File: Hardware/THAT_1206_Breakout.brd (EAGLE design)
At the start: 45.7 x 20.3 mm, 32 parts, among them IC1 THAT1206, J1 INPUT, J2 CHASSIS, J3 RN, J4 TN, J5 SN, J6 1x4, J7 R, J8 T

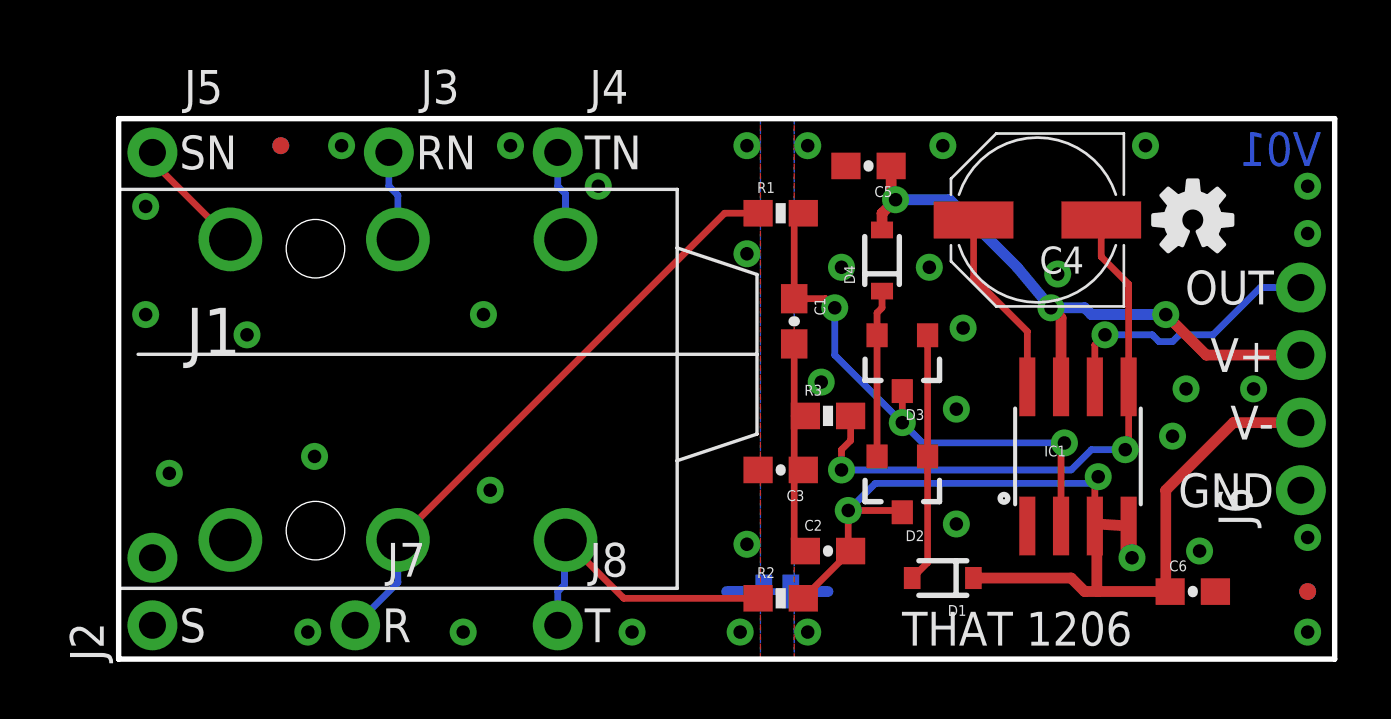
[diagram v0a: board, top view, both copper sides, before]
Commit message: Moving PTH holes to 0.1" grid, matching size to 1646 board.
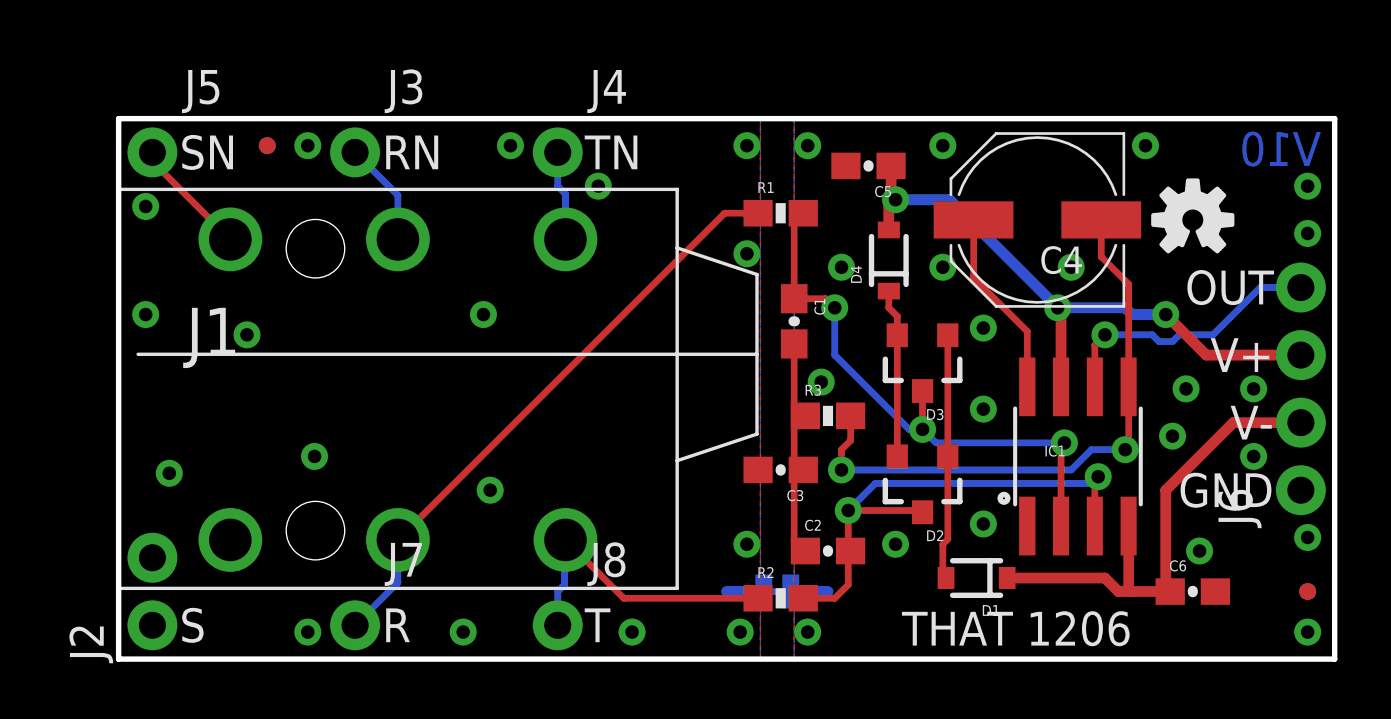
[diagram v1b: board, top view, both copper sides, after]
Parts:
- moved D1 1.27 mm to (32.3, 3.05)
- moved J3 1.27 mm to (8.89, 19.1)
- moved D2 0.76 mm to (30.2, 6.62)
- moved D3 0.76 mm to (30.2, 11.2)
- moved FD2 0.51 mm to (5.59, 19.3)
- moved FD3 0.51 mm to (5.59, 19.3)
- moved D4 0.25 mm to (29.0, 15.0)
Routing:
- net VNEG: track 21.4 -> 18.9 mm
- net N$4: track 18.0 -> 19.4 mm
- net N$10: track 3.41 -> 3.94 mm
- net GND: vias 20 -> 21
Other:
- board text added: "V10"
- board text removed: "V01"

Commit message: Updates after group review.
-Chassis ground moved out of selective solder runout path.
-Flame turned right side up.
-A few via/silk overlaps fixed.
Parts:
- added J9: Chassis, SparkFun-Connectors:1X01_NO_SILK
- J2: value CHASSIS -> S; device SparkFun-Connectors:1X02_NO_SILK -> SparkFun-Connectors:1X01_NO_SILK
- moved LOGO2 4.91 mm to (10.9, 7.62), turned to 0 degrees
- turned J2 to 0 degrees
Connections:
- net GND-ISO: now also J9.1; no longer J2.2
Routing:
- net GND: vias 21 -> 22
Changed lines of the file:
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@@
 <setting verticaltext="up"/>
 </settings>
-<grid distance="0.1" unitdist="inch" unit="inch" style="lines" multiple="1" display="yes" altdistance="0.01" altunitdist="inch" altunit="inch"/>
+<grid distance="0.05" unitdist="inch" unit="inch" style="lines" multiple="1" display="yes" altdistance="0.005" altunitdist="inch" altunit="inch"/>
 <layers>
 <layer number="1" name="Top" color="4" fill="1" visible="yes" active="yes"/>
@@
 <layer number="45" name="Holes" color="7" fill="1" visible="no" active="yes"/>
 <layer number="46" name="Milling" color="3" fill="1" visible="no" active="yes"/>
-<layer number="47" name="Measures" color="7" fill="1" visible="yes" active="yes"/>
+<layer number="47" name="Measures" color="7" fill="1" visible="no" active="yes"/>
 <layer number="48" name="Document" color="7" fill="1" visible="no" active="yes"/>
 <layer number="49" name="Reference" color="7" fill="1" visible="no" active="yes"/>
@@
 Line Receiver
 Breakout</text>
-<text x="1.27" y="4.826" size="1.27" layer="22" font="vector" ratio="15" rot="MR90" align="center-left">Chassis</text>
+<text x="1.27" y="2.54" size="1.27" layer="22" font="vector" ratio="15" rot="MR90" align="center-left">Chassis</text>
 <text x="26.162" y="0.508" size="1.016" layer="22" font="vector" ratio="15" rot="MR0" align="bottom-right">Cut jumper to
 isolate chassis
@@
 <attribute name="PROD_ID" value="CAP-08604" x="40.386" y="2.54" size="1.778" layer="27" font="vector" ratio="15" display="off"/>
 </element>
-<element name="J2" library="SparkFun-Connectors" package="1X02_NO_SILK" value="CHASSIS" x="1.27" y="1.27" rot="R90"/>
 <element name="J6" library="SparkFun-Connectors" package="1X04_NO_SILK_ALL_ROUND" value="1x4" x="44.45" y="6.35" rot="R90">
 <attribute name="PROD_ID" value="CONN-09696" x="44.45" y="6.35" size="1.778" layer="27" font="vector" ratio="15" rot="R90" display="off"/>
@@
 <element name="FD3" library="SparkFun-Aesthetics" package="MICRO-FIDUCIAL" value="FIDUCIALUFIDUCIAL" x="5.588" y="19.304"/>
 <element name="FD4" library="SparkFun-Aesthetics" package="MICRO-FIDUCIAL" value="FIDUCIALUFIDUCIAL" x="44.704" y="2.54"/>
-<element name="LOGO2" library="SparkFun-Aesthetics" package="SFE_LOGO_FLAME_.2" value="SFE_LOGO_FLAME.2_INCH" x="12.7" y="12.192" rot="MR270"/>
+<element name="LOGO2" library="SparkFun-Aesthetics" package="SFE_LOGO_FLAME_.2" value="SFE_LOGO_FLAME.2_INCH" x="10.922" y="7.62" rot="MR0"/>
 <element name="FD1" library="SparkFun-Aesthetics" package="MICRO-FIDUCIAL" value="FIDUCIALUFIDUCIAL" x="44.704" y="2.54" rot="MR0"/>
 <element name="FD2" library="SparkFun-Aesthetics" package="MICRO-FIDUCIAL" value="FIDUCIALUFIDUCIAL" x="5.588" y="19.304" rot="MR90"/>
@@
 <element name="J7" library="SparkFun-Connectors" package="1X01_NO_SILK" value="R" x="8.89" y="1.27"/>
 <element name="J8" library="SparkFun-Connectors" package="1X01_NO_SILK" value="T" x="16.51" y="1.27"/>
+<element name="J2" library="SparkFun-Connectors" package="1X01_NO_SILK" value="S" x="1.27" y="1.27"/>
+<element name="J9" library="SparkFun-Connectors" package="1X01_NO_SILK" value="Chassis" x="1.27" y="11.43"/>
 </elements>
 <signals>
@@
 <via x="32.512" y="12.446" extent="1-16" drill="0.508"/>
 <via x="32.512" y="9.398" extent="1-16" drill="0.508"/>
-<via x="29.21" y="4.318" extent="1-16" drill="0.508"/>
+<via x="28.956" y="3.302" extent="1-16" drill="0.508"/>
 <via x="25.908" y="1.016" extent="1-16" drill="0.508"/>
 <via x="40.64" y="4.064" extent="1-16" drill="0.508"/>
@@
 <via x="26.416" y="10.414" extent="1-16" drill="0.508"/>
 <via x="32.512" y="5.08" extent="1-16" drill="0.508"/>
+<via x="33.147" y="1.524" extent="1-16" drill="0.508"/>
 </signal>
 <signal name="VCC">
@@
 <contactref element="C3" pad="2"/>
 <contactref element="J1" pad="SLEEVE"/>
-<contactref element="J2" pad="2"/>
-<contactref element="J2" pad="1"/>
 <polygon width="0.254" layer="16" isolate="0.3048">
 <vertex x="0" y="20.32"/>
@@
 <via x="7.366" y="7.62" extent="1-16" drill="0.508"/>
 <via x="1.016" y="12.954" extent="1-16" drill="0.508"/>
-<via x="1.905" y="6.985" extent="1-16" drill="0.508"/>
+<via x="2.159" y="7.366" extent="1-16" drill="0.508"/>
 <via x="7.112" y="1.016" extent="1-16" drill="0.508"/>
 <via x="12.954" y="1.016" extent="1-16" drill="0.508"/>
@@
 <via x="14.732" y="19.304" extent="1-16" drill="0.508"/>
 <via x="19.304" y="1.016" extent="1-16" drill="0.508"/>
+<contactref element="J2" pad="1"/>
+<contactref element="J9" pad="1"/>
 </signal>
 <signal name="RCV">

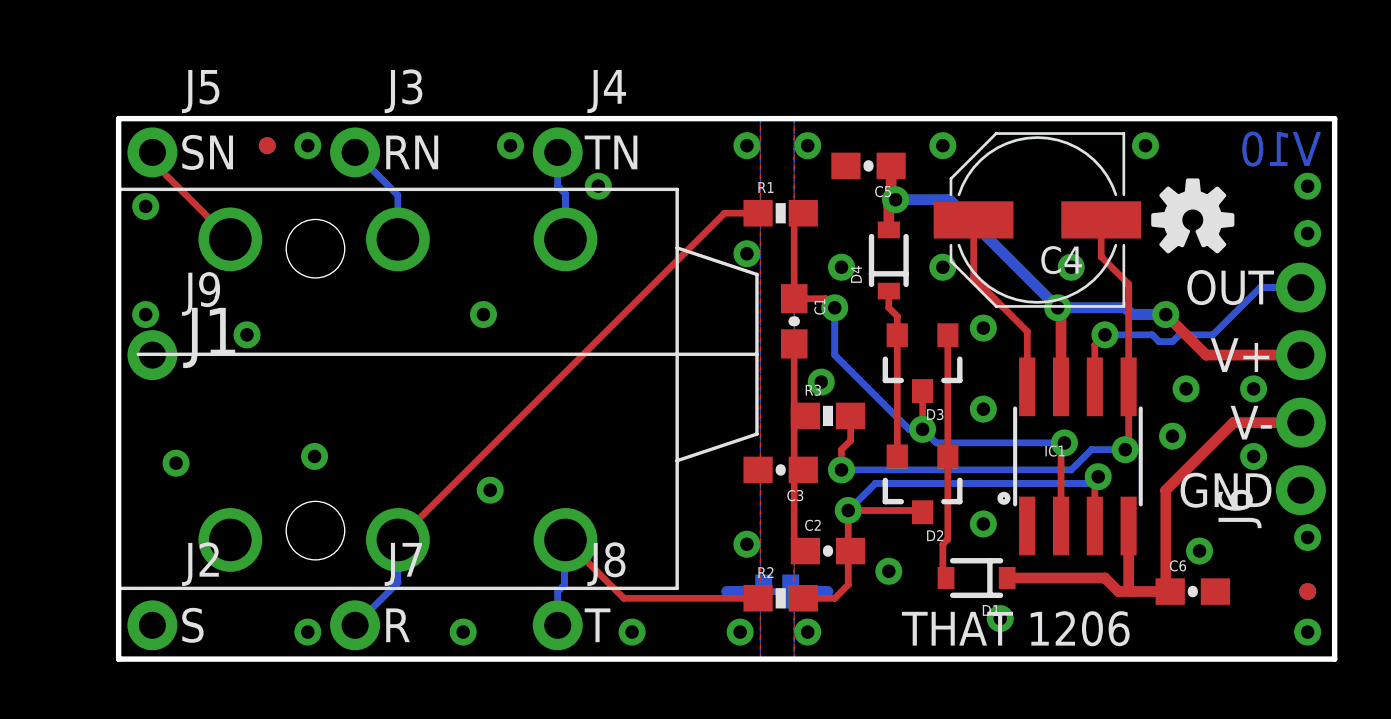
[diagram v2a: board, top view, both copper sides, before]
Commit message: Updated after running checklist.
Biggest change is that TRS jack was updated with new libraries.
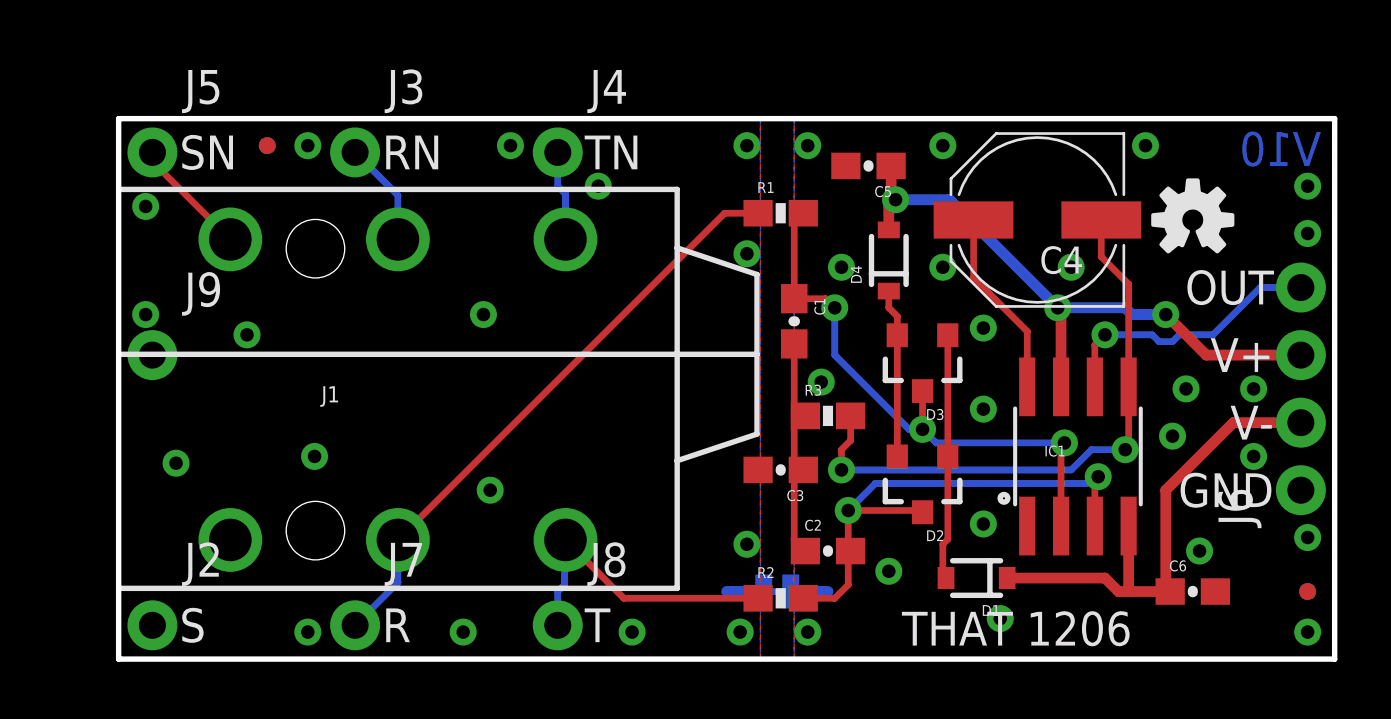
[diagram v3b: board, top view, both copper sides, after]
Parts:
- J1: device SparkFun-Connectors:AUDIO-JACK-.25-INCH-HORIZ-PTH -> SparkFun-Connectors:AUDIO_JACK_0.25"_TRS_PTH_RA
- moved FD1 42.6 mm to (5.59, 19.3)
- moved FD2 42.6 mm to (44.7, 2.54), turned to 0 degrees
- renumbered LOGO6 to LOGO5
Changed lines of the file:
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@@
 <layer number="20" name="Dimension" color="15" fill="1" visible="yes" active="yes"/>
 <layer number="21" name="tPlace" color="16" fill="1" visible="yes" active="yes"/>
-<layer number="22" name="bPlace" color="14" fill="1" visible="no" active="yes"/>
+<layer number="22" name="bPlace" color="14" fill="1" visible="yes" active="yes"/>
 <layer number="23" name="tOrigins" color="15" fill="1" visible="yes" active="yes"/>
 <layer number="24" name="bOrigins" color="15" fill="1" visible="no" active="yes"/>
-<layer number="25" name="tNames" color="7" fill="1" visible="yes" active="yes"/>
+<layer number="25" name="tNames" color="7" fill="1" visible="no" active="yes"/>
 <layer number="26" name="bNames" color="7" fill="1" visible="no" active="yes"/>
 <layer number="27" name="tValues" color="7" fill="1" visible="no" active="yes"/>
@@
 <layer number="37" name="tTest" color="7" fill="1" visible="no" active="yes"/>
 <layer number="38" name="bTest" color="7" fill="1" visible="no" active="yes"/>
-<layer number="39" name="tKeepout" color="4" fill="11" visible="no" active="yes"/>
-<layer number="40" name="bKeepout" color="1" fill="11" visible="no" active="yes"/>
+<layer number="39" name="tKeepout" color="4" fill="11" visible="yes" active="yes"/>
+<layer number="40" name="bKeepout" color="1" fill="11" visible="yes" active="yes"/>
 <layer number="41" name="tRestrict" color="4" fill="10" visible="no" active="yes"/>
 <layer number="42" name="bRestrict" color="1" fill="10" visible="no" active="yes"/>
@@
 <layer number="45" name="Holes" color="7" fill="1" visible="no" active="yes"/>
 <layer number="46" name="Milling" color="3" fill="1" visible="no" active="yes"/>
-<layer number="47" name="Measures" color="7" fill="1" visible="no" active="yes"/>
+<layer number="47" name="Measures" color="7" fill="1" visible="yes" active="yes"/>
 <layer number="48" name="Document" color="7" fill="1" visible="no" active="yes"/>
 <layer number="49" name="Reference" color="7" fill="1" visible="no" active="yes"/>
 <layer number="50" name="dxf" color="7" fill="1" visible="no" active="no"/>
-<layer number="51" name="tDocu" color="6" fill="1" visible="no" active="yes"/>
+<layer number="51" name="tDocu" color="6" fill="1" visible="yes" active="yes"/>
 <layer number="52" name="bDocu" color="7" fill="1" visible="no" active="yes"/>
 <layer number="53" name="tGND_GNDA" color="7" fill="9" visible="no" active="no"/>
@@
 <attribute name="PROD_ID" value="IC-13469" x="36.068" y="7.62" size="1.778" layer="27" display="off"/>
 </element>
-<element name="J1" library="SparkFun-Connectors" package="AUDIO-JACK-.25-INCH-HORIZ-PTH" value="INPUT" x="0" y="11.43">
+<element name="J1" library="SparkFun-Connectors" package="AUDIO_JACK_0.25&quot;_TRS_PTH_RA" value="INPUT" x="0" y="11.43">
 <attribute name="PROD_ID" value="CONN-12339" x="0" y="11.43" size="1.778" layer="27" display="off"/>
 <attribute name="SF_ID" value="COM-11144" x="0" y="11.43" size="1.778" layer="27" display="off"/>
@@
 <element name="FD4" library="SparkFun-Aesthetics" package="MICRO-FIDUCIAL" value="FIDUCIALUFIDUCIAL" x="44.704" y="2.54"/>
 <element name="LOGO2" library="SparkFun-Aesthetics" package="SFE_LOGO_FLAME_.2" value="SFE_LOGO_FLAME.2_INCH" x="10.922" y="7.62" rot="MR0"/>
-<element name="FD1" library="SparkFun-Aesthetics" package="MICRO-FIDUCIAL" value="FIDUCIALUFIDUCIAL" x="44.704" y="2.54" rot="MR0"/>
-<element name="FD2" library="SparkFun-Aesthetics" package="MICRO-FIDUCIAL" value="FIDUCIALUFIDUCIAL" x="5.588" y="19.304" rot="MR90"/>
 <element name="J3" library="SparkFun-Connectors" package="1X01_NO_SILK" value="RN" x="8.89" y="19.05"/>
 <element name="J4" library="SparkFun-Connectors" package="1X01_NO_SILK" value="TN" x="16.51" y="19.05"/>
 <element name="J5" library="SparkFun-Connectors" package="1X01_NO_SILK" value="SN" x="1.27" y="19.05"/>
-<element name="LOGO6" library="SparkFun-Aesthetics" package="SFE_LOGO_NAME_.1" value="SFE_LOGO_NAME.1_INCH" x="38.735" y="13.97" rot="MR0"/>
 <element name="J7" library="SparkFun-Connectors" package="1X01_NO_SILK" value="R" x="8.89" y="1.27"/>
 <element name="J8" library="SparkFun-Connectors" package="1X01_NO_SILK" value="T" x="16.51" y="1.27"/>
 <element name="J2" library="SparkFun-Connectors" package="1X01_NO_SILK" value="S" x="1.27" y="1.27"/>
 <element name="J9" library="SparkFun-Connectors" package="1X01_NO_SILK" value="Chassis" x="1.27" y="11.43"/>
+<element name="LOGO5" library="SparkFun-Aesthetics" package="SFE_LOGO_NAME_.1" value="SFE_LOGO_NAME.1_INCH" x="38.735" y="13.97" rot="MR0"/>
+<element name="FD1" library="SparkFun-Aesthetics" package="MICRO-FIDUCIAL" value="FIDUCIALUFIDUCIAL" x="5.588" y="19.304" rot="MR0"/>
+<element name="FD2" library="SparkFun-Aesthetics" package="MICRO-FIDUCIAL" value="FIDUCIALUFIDUCIAL" x="44.704" y="2.54" rot="MR0"/>
 </elements>
 <signals>
